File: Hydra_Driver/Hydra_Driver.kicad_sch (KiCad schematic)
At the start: 43 parts, among them IC1 ESP32-S3-WROOM-1-N4, J1 USB4105-GF-A, J10 Conn_01x03, J11 Conn_01x04, J12 Conn_01x03, J13 Conn_01x02, J2 Conn_01x02, J3 Conn_01x06, J4 Conn_01x03, J5 Conn_01x04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

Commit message: Started making some changes based on design review
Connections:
- net IN1HA renamed EN1A
- net IN1HB renamed EN1B
- net IN1LA renamed IN1A
- net IN1LB renamed IN1B
- net IN2HA renamed EN2A
- net IN2HB renamed EN2B
- net IN2LA renamed IN2A
- net IN2LB renamed IN2B
- net IN3HA renamed EN3A
- net IN3HB renamed EN3B
- net IN3LA renamed IN3A
- net IN3LB renamed IN3B
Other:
- sheet Driver_Unit ports: added EN1, EN2, EN3, IN1, IN2, IN3; removed IN1H, IN1L, IN2H, IN2L, IN3H, IN3L
- sheet Driver_Unit1 ports: added EN1, EN2, EN3, IN1, IN2, IN3; removed IN1H, IN1L, IN2H, IN2L, IN3H, IN3L

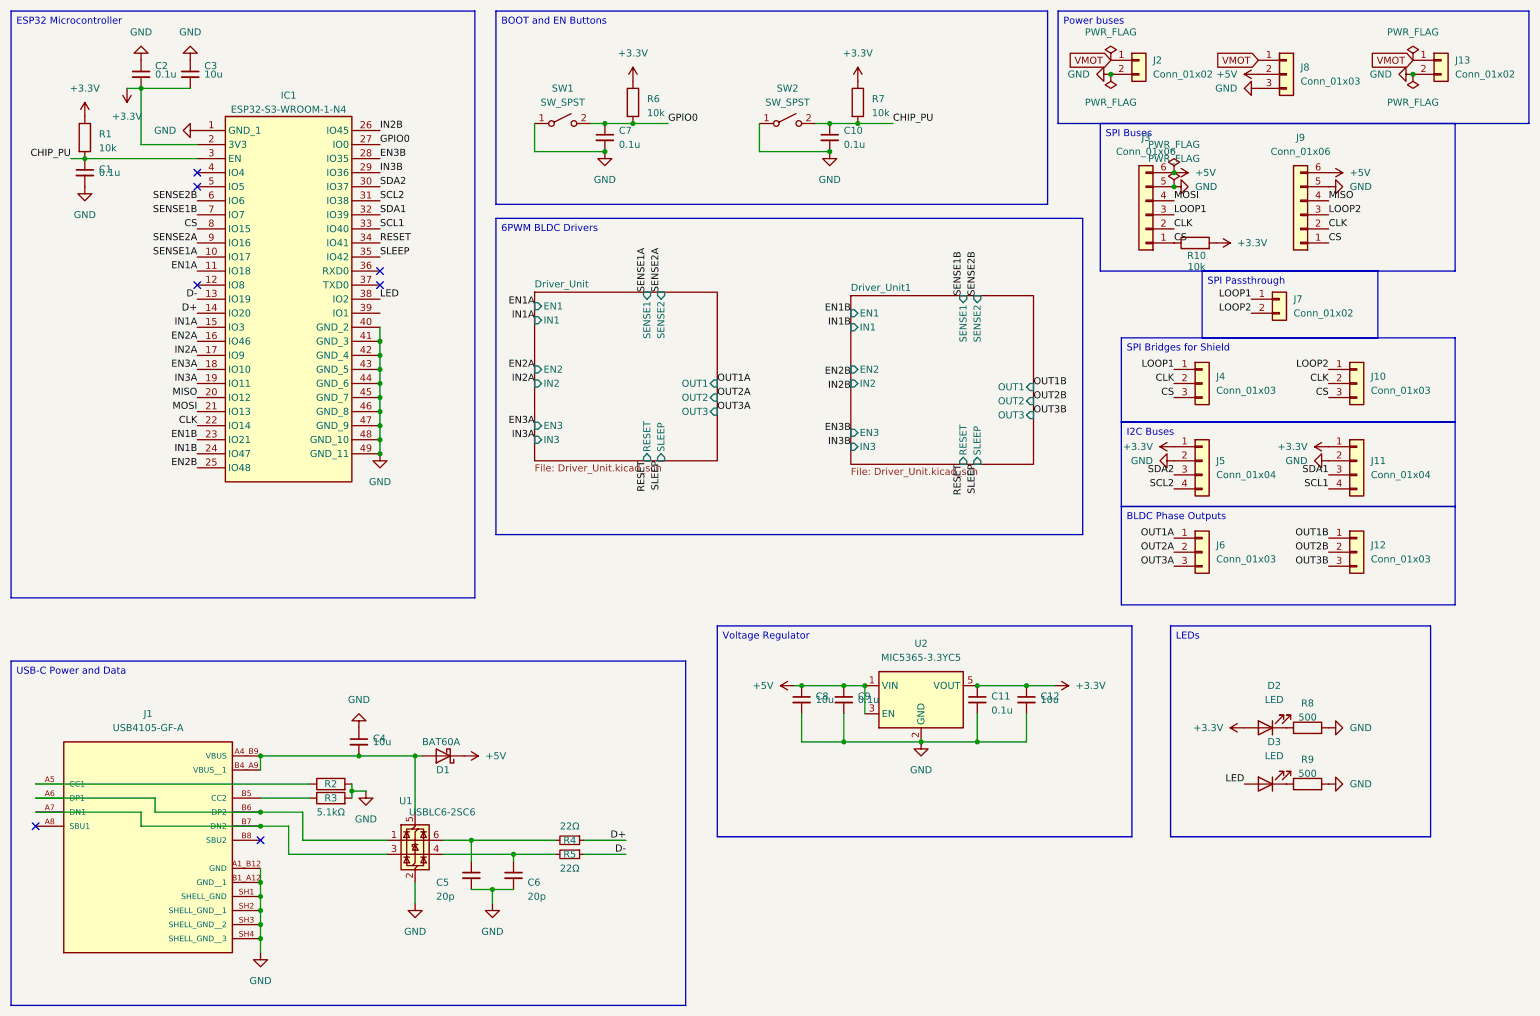
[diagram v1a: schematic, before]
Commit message: Mostly finished applying changes from design review
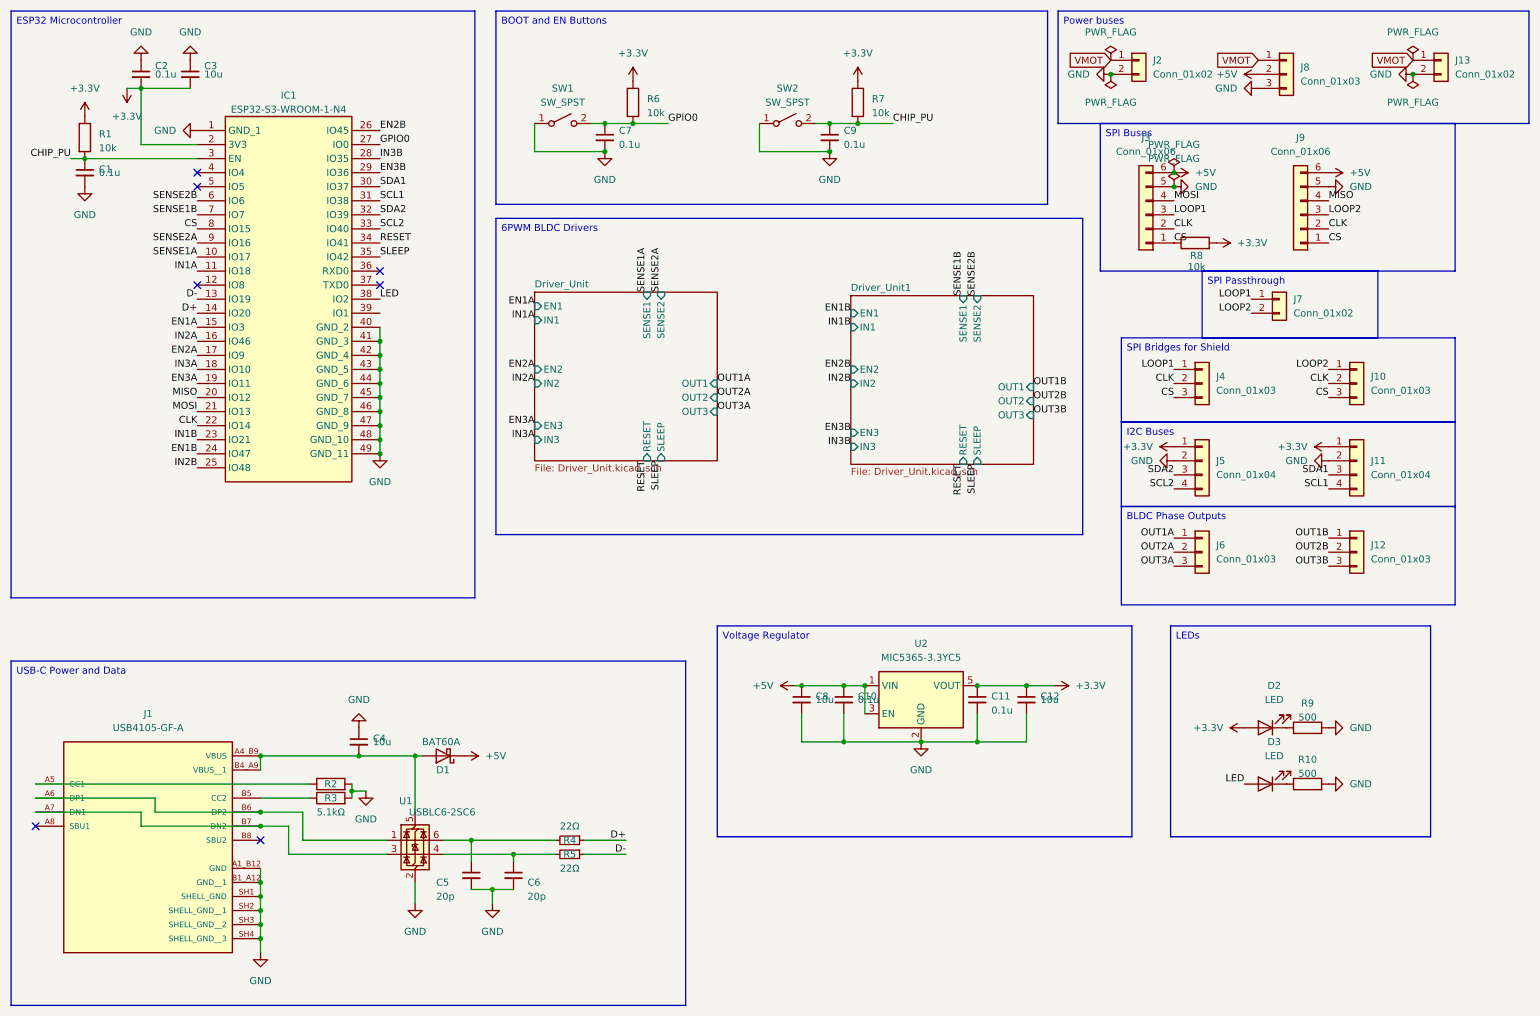
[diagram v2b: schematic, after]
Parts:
- J11, J5: footprint Connector_PinHeader_2.54mm:PinHeader_1x04_P2.54mm_Vertical -> Connector_PinHeader_2.54mm:PinHeader_1x04_P2.54mm_Horizontal
- J12, J6: footprint Connector_PinHeader_2.54mm:PinHeader_1x03_P2.54mm_Vertical -> Connector_PinHeader_2.54mm:PinHeader_1x03_P2.54mm_Horizontal
- renumbered C9 to C10, C10 to C9, R9 to R10, R10 to R8, R8 to R9
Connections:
- net EN1A: now also IC1.15 (IO3); no longer IC1.11 (IO18)
- net EN1B: now also IC1.24 (IO47); no longer IC1.23 (IO21)
- net EN2A: now also IC1.17 (IO9); no longer IC1.16 (IO46)
- net EN2B: now also IC1.26 (IO45); no longer IC1.25 (IO48)
- net EN3A: now also IC1.19 (IO11); no longer IC1.18 (IO10)
- net EN3B: now also IC1.29 (IO36); no longer IC1.28 (IO35)
- net IN1A: now also IC1.11 (IO18); no longer IC1.15 (IO3)
- net IN1B: now also IC1.23 (IO21); no longer IC1.24 (IO47)
- net IN2A: now also IC1.16 (IO46); no longer IC1.17 (IO9)
- net IN2B: now also IC1.25 (IO48); no longer IC1.26 (IO45)
- net IN3A: now also IC1.18 (IO10); no longer IC1.19 (IO11)
- net IN3B: now also IC1.28 (IO35); no longer IC1.29 (IO36)
- net SCL1: now also IC1.31 (IO38); no longer IC1.33 (IO40)
- net SCL2: now also IC1.33 (IO40); no longer IC1.31 (IO38)
- net SDA1: now also IC1.30 (IO37); no longer IC1.32 (IO39)
- net SDA2: now also IC1.32 (IO39); no longer IC1.30 (IO37)

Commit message: Finished Hydra modifications
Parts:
- removed U2: MIC5365-3.3YC5, Package_TO_SOT_SMD:SOT-353_SC-70-5, symbol Regulator_Linear:MIC5365-3.3YC5
- added U2: MIC5504-3.3YM5-TR, Touchstone:SOT-23-5_MC_MCH, symbol MIC5504:MIC5504-3.3YM5-TR
- renumbered C9 to C10, C10 to C9
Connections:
- net +3.3V: now also U2.5 (VOUT)
- net +5V: now also U2.1 (VIN), U2.3 (EN)
- net GND: now also U2.2 (GND)
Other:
- moved on the sheet: C11, C12, C8, C9

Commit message: Changed shield passthrough to pin header
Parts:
- J7: footprint Connector_PinSocket_2.54mm:PinSocket_1x02_P2.54mm_Vertical -> Connector_PinHeader_2.54mm:PinHeader_1x02_P2.54mm_Vertical
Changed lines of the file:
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@@
 			)
 		)
-		(property "Footprint" "Connector_PinSocket_2.54mm:PinSocket_1x02_P2.54mm_Vertical"
+		(property "Footprint" "Connector_PinHeader_2.54mm:PinHeader_1x02_P2.54mm_Vertical"
 			(at 243.84 64.77 0)
 			(effects
